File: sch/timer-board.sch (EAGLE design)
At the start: 37 parts, among them T1 2N3904, U2 328P

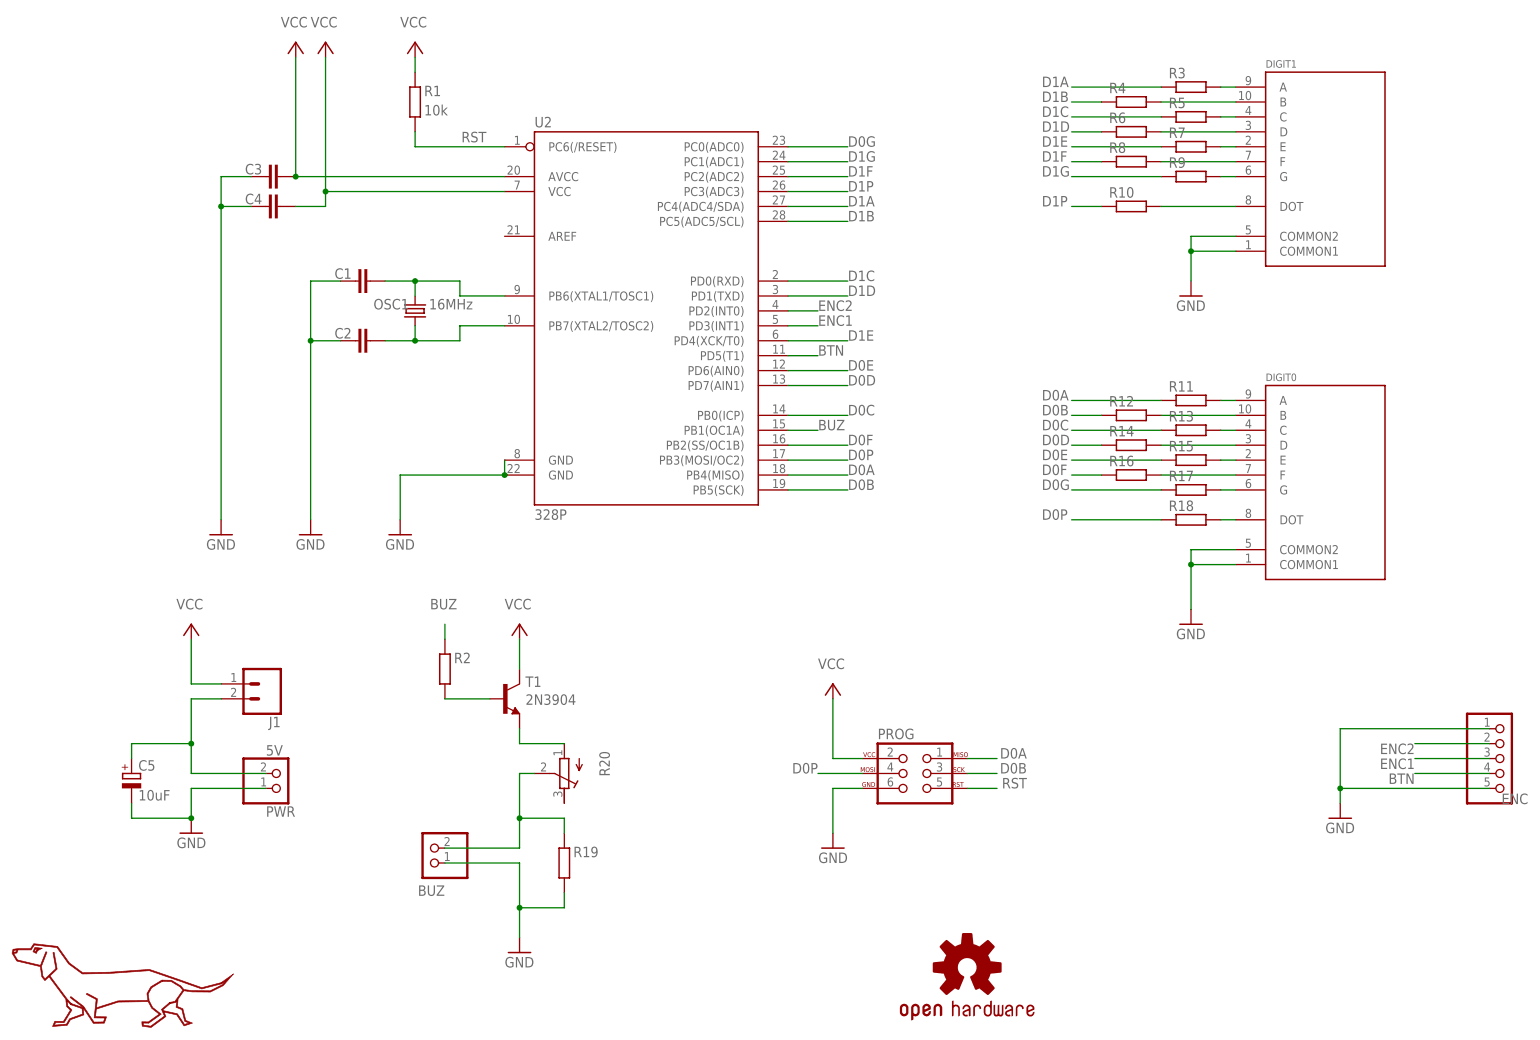
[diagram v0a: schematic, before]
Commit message: refactoring: added vcc pour, updated capacitors footprints fix: correct orientation of 7segment displays
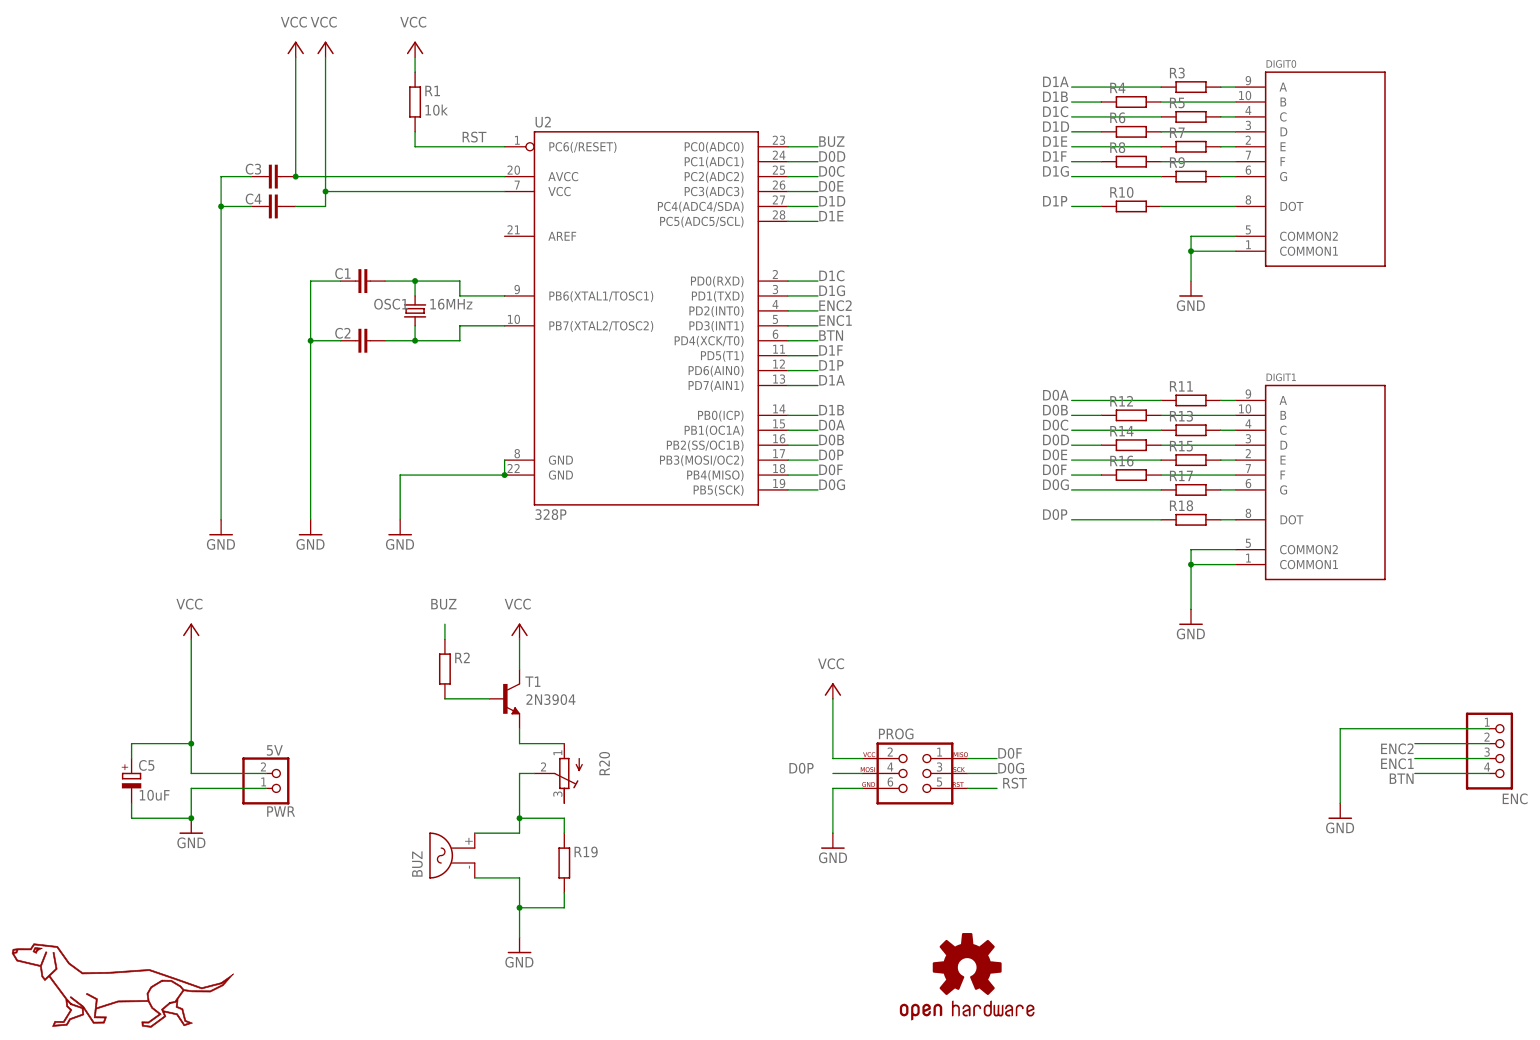
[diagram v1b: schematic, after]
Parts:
- removed J1: (no value), SparkFun-Connectors:CONN_02LOCK
- BUZ: value CONN_1X2JST -> BUZZER; device parts:CONN_1X2JST -> parts:BUZZER
- C1, C2, C3, C4: device rcl:C-EU050-024X044 -> rcl:C-EU025-024X044
- ENC: device parts:CONN_1X5JST -> parts:CONN_1X4
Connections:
- removed net N$11: C5.+, J1.2, PWR.2
- net BTN: now also U2.PD4(XCK/T0); no longer U2.PD5(T1)
- net BUZ: now also U2.PC0(ADC0); no longer U2.PB1(OC1A)
- net D0A: now also U2.PB1(OC1A); no longer PROG.1, U2.PB4(MISO)
- net D0B: now also U2.PB2(SS/OC1B); no longer PROG.3, U2.PB5(SCK)
- net D0C: now also U2.PC2(ADC2); no longer U2.PB0(ICP)
- net D0D: now also U2.PC1(ADC1); no longer U2.PD7(AIN1)
- net D0E: now also U2.PC3(ADC3); no longer U2.PD6(AIN0)
- net D0F: now also PROG.1, U2.PB4(MISO); no longer U2.PB2(SS/OC1B)
- net D0G: now also PROG.3, U2.PB5(SCK); no longer U2.PC0(ADC0)
- net D1A: now also U2.PD7(AIN1); no longer U2.PC4(ADC4/SDA)
- net D1B: now also U2.PB0(ICP); no longer U2.PC5(ADC5/SCL)
- net D1D: now also U2.PC4(ADC4/SDA); no longer U2.PD1(TXD)
- net D1E: now also U2.PC5(ADC5/SCL); no longer U2.PD4(XCK/T0)
- net D1F: now also U2.PD5(T1); no longer U2.PC2(ADC2)
- net D1G: now also U2.PD1(TXD); no longer U2.PC1(ADC1)
- net D1P: now also U2.PD6(AIN0); no longer U2.PC3(ADC3)
- net GND: no longer ENC.5
- net N$1: now also DIGIT0.A; no longer DIGIT1.A
- net N$13: now also DIGIT1.A; no longer DIGIT0.A
- net N$14: now also DIGIT1.B; no longer DIGIT0.B
- net N$15: now also DIGIT1.C; no longer DIGIT0.C
- net N$16: now also DIGIT1.D; no longer DIGIT0.D
- net N$17: now also DIGIT1.E; no longer DIGIT0.E
- net N$18: now also DIGIT1.F; no longer DIGIT0.F
- net N$19: now also DIGIT1.G; no longer DIGIT0.G
- net N$2: now also DIGIT0.B; no longer DIGIT1.B
- net N$20: now also DIGIT1.DOT; no longer DIGIT0.DOT
- net N$3: now also DIGIT0.C; no longer DIGIT1.C
- net N$4: now also DIGIT0.D; no longer DIGIT1.D
- net N$5: now also DIGIT0.E; no longer DIGIT1.E
- net N$6: now also DIGIT0.F; no longer DIGIT1.F
- net N$7: now also DIGIT0.G; no longer DIGIT1.G
- net N$9: now also DIGIT0.DOT; no longer DIGIT1.DOT
- net VCC: now also C5.+, PWR.2; no longer J1.1
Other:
- moved on the sheet: BUZ, DIGIT0, DIGIT1

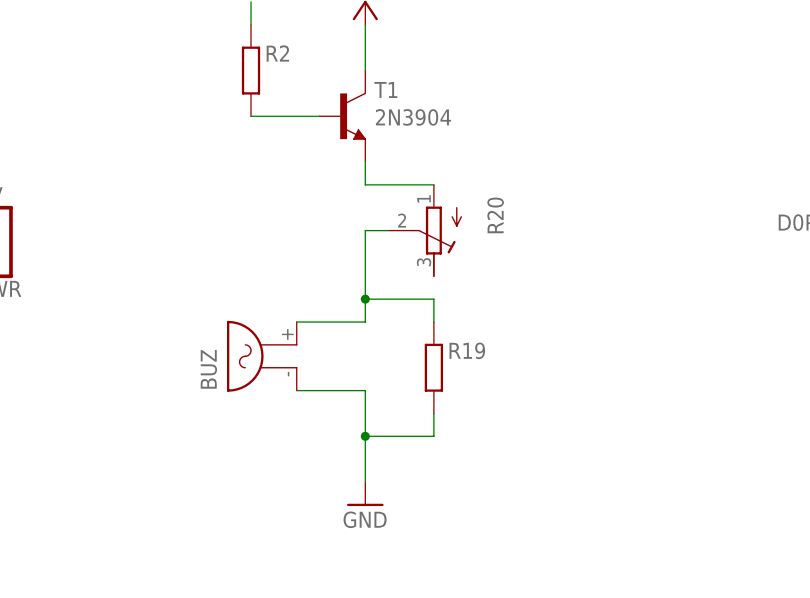
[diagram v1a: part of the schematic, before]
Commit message: fix: clearance around milling, moved resistors, removed buzzer resistor
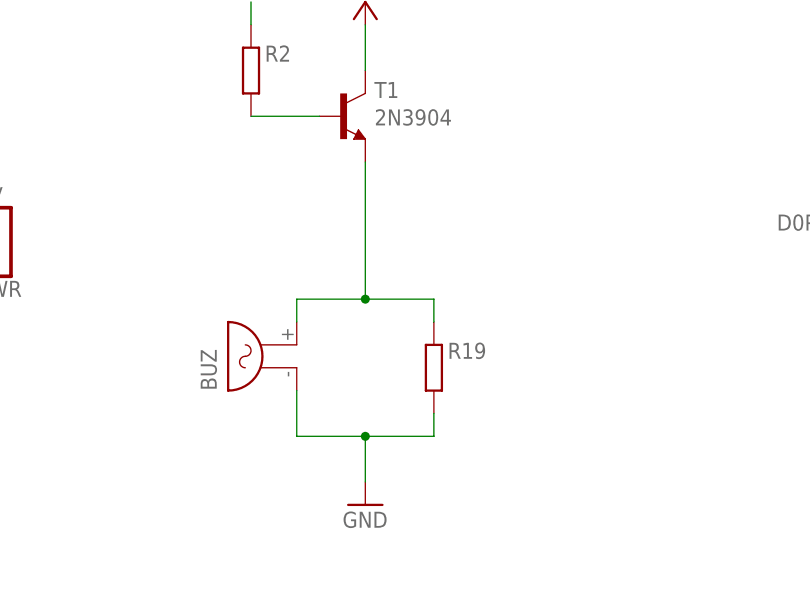
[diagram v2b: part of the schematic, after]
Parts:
- removed R20: (no value), rcl:R-TRIMM3296W
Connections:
- removed net N$12: R20.A, T1.E
- net N$21: now also T1.E; no longer R20.S
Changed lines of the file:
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@@
 <?xml version="1.0" encoding="utf-8"?>
 <!DOCTYPE eagle SYSTEM "eagle.dtd">
-<eagle version="9.5.0">
+<eagle version="9.6.1">
 <drawing>
 <settings>
-<setting alwaysvectorfont="no"/>
+<setting alwaysvectorfont="yes"/>
 <setting verticaltext="up"/>
 </settings>
@@
 <part name="FRAME1" library="SparkFun-Aesthetics" library_urn="urn:adsk.eagle:library:507" deviceset="FRAME-A4L" device="">
 <attribute name="CNAME" value="Arduino timer"/>
-<attribute name="CREVISION" value="3"/>
+<attribute name="CREVISION" value="4"/>
 <attribute name="DESIGNER" value="Mathieu Brun"/>
 </part>
@@
 <part name="BUZ" library="parts" deviceset="BUZZER" device=""/>
 <part name="R19" library="rcl" library_urn="urn:adsk.eagle:library:334" deviceset="R-EU_" device="0207/10" package3d_urn="urn:adsk.eagle:package:23491/1"/>
-<part name="R20" library="rcl" library_urn="urn:adsk.eagle:library:334" deviceset="R-TRIMM" device="3296W" package3d_urn="urn:adsk.eagle:package:26033/1"/>
 <part name="U2" library="SparkFun-IC-Microcontroller" library_urn="urn:adsk.eagle:library:525" deviceset="ATMEGA328P_PDIP" device="" package3d_urn="urn:adsk.eagle:package:38942/1" value="328P"/>
 <part name="P+6" library="supply1" library_urn="urn:adsk.eagle:library:371" deviceset="VCC" device=""/>
@@
 <attribute name="VALUE" x="-27.178" y="-52.07" size="1.778" layer="96" rot="R90"/>
 </instance>
-<instance part="R20" gate="G$1" x="-30.48" y="-33.02" smashed="yes" rot="R180">
-<attribute name="NAME" x="-24.511" y="-29.21" size="1.778" layer="95" rot="R270"/>
-<attribute name="VALUE" x="-26.67" y="-29.21" size="1.778" layer="96" rot="R270"/>
-</instance>
 <instance part="U2" gate="G$1" x="-17.78" y="48.26" smashed="yes">
 <attribute name="NAME" x="-35.56" y="76.962" size="1.778" layer="95"/>
@@
 <segment>
 <pinref part="BUZ" gate="G$1" pin="1"/>
-<wire x1="-45.72" y1="-50.8" x2="-38.1" y2="-50.8" width="0.1524" layer="91"/>
+<wire x1="-45.72" y1="-50.8" x2="-45.72" y2="-55.88" width="0.1524" layer="91"/>
 <pinref part="GND1" gate="1" pin="GND"/>
 <wire x1="-38.1" y1="-60.96" x2="-38.1" y2="-55.88" width="0.1524" layer="91"/>
 <pinref part="R19" gate="G$1" pin="1"/>
-<wire x1="-38.1" y1="-55.88" x2="-38.1" y2="-50.8" width="0.1524" layer="91"/>
+<wire x1="-38.1" y1="-55.88" x2="-45.72" y2="-55.88" width="0.1524" layer="91"/>
 <wire x1="-30.48" y1="-53.34" x2="-30.48" y2="-55.88" width="0.1524" layer="91"/>
 <wire x1="-30.48" y1="-55.88" x2="-38.1" y2="-55.88" width="0.1524" layer="91"/>
@@
 </segment>
 </net>
-<net name="N$12" class="0">
-<segment>
-<pinref part="T1" gate="G1" pin="E"/>
-<wire x1="-38.1" y1="-25.4" x2="-38.1" y2="-27.94" width="0.1524" layer="91"/>
-<pinref part="R20" gate="G$1" pin="A"/>
-<wire x1="-38.1" y1="-27.94" x2="-30.48" y2="-27.94" width="0.1524" layer="91"/>
-</segment>
-</net>
 <net name="N$21" class="0">
 <segment>
-<pinref part="R20" gate="G$1" pin="S"/>
-<wire x1="-35.56" y1="-33.02" x2="-38.1" y2="-33.02" width="0.1524" layer="91"/>
 <pinref part="BUZ" gate="G$1" pin="2"/>
-<wire x1="-38.1" y1="-40.64" x2="-38.1" y2="-43.18" width="0.1524" layer="91"/>
-<wire x1="-45.72" y1="-43.18" x2="-38.1" y2="-43.18" width="0.1524" layer="91"/>
+<wire x1="-38.1" y1="-40.64" x2="-45.72" y2="-40.64" width="0.1524" layer="91"/>
+<wire x1="-45.72" y1="-43.18" x2="-45.72" y2="-40.64" width="0.1524" layer="91"/>
 <pinref part="R19" gate="G$1" pin="2"/>
 <wire x1="-30.48" y1="-43.18" x2="-30.48" y2="-40.64" width="0.1524" layer="91"/>
 <wire x1="-30.48" y1="-40.64" x2="-38.1" y2="-40.64" width="0.1524" layer="91"/>
-<wire x1="-38.1" y1="-33.02" x2="-38.1" y2="-40.64" width="0.1524" layer="91"/>
 <junction x="-38.1" y="-40.64"/>
-</segment>
-</net>
+<pinref part="T1" gate="G1" pin="E"/>
+<wire x1="-38.1" y1="-40.64" x2="-38.1" y2="-25.4" width="0.1524" layer="91"/>
+</segment>
+</net>
